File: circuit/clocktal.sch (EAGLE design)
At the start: 28 parts, among them IC1 PIC16F688, Q1 8.0

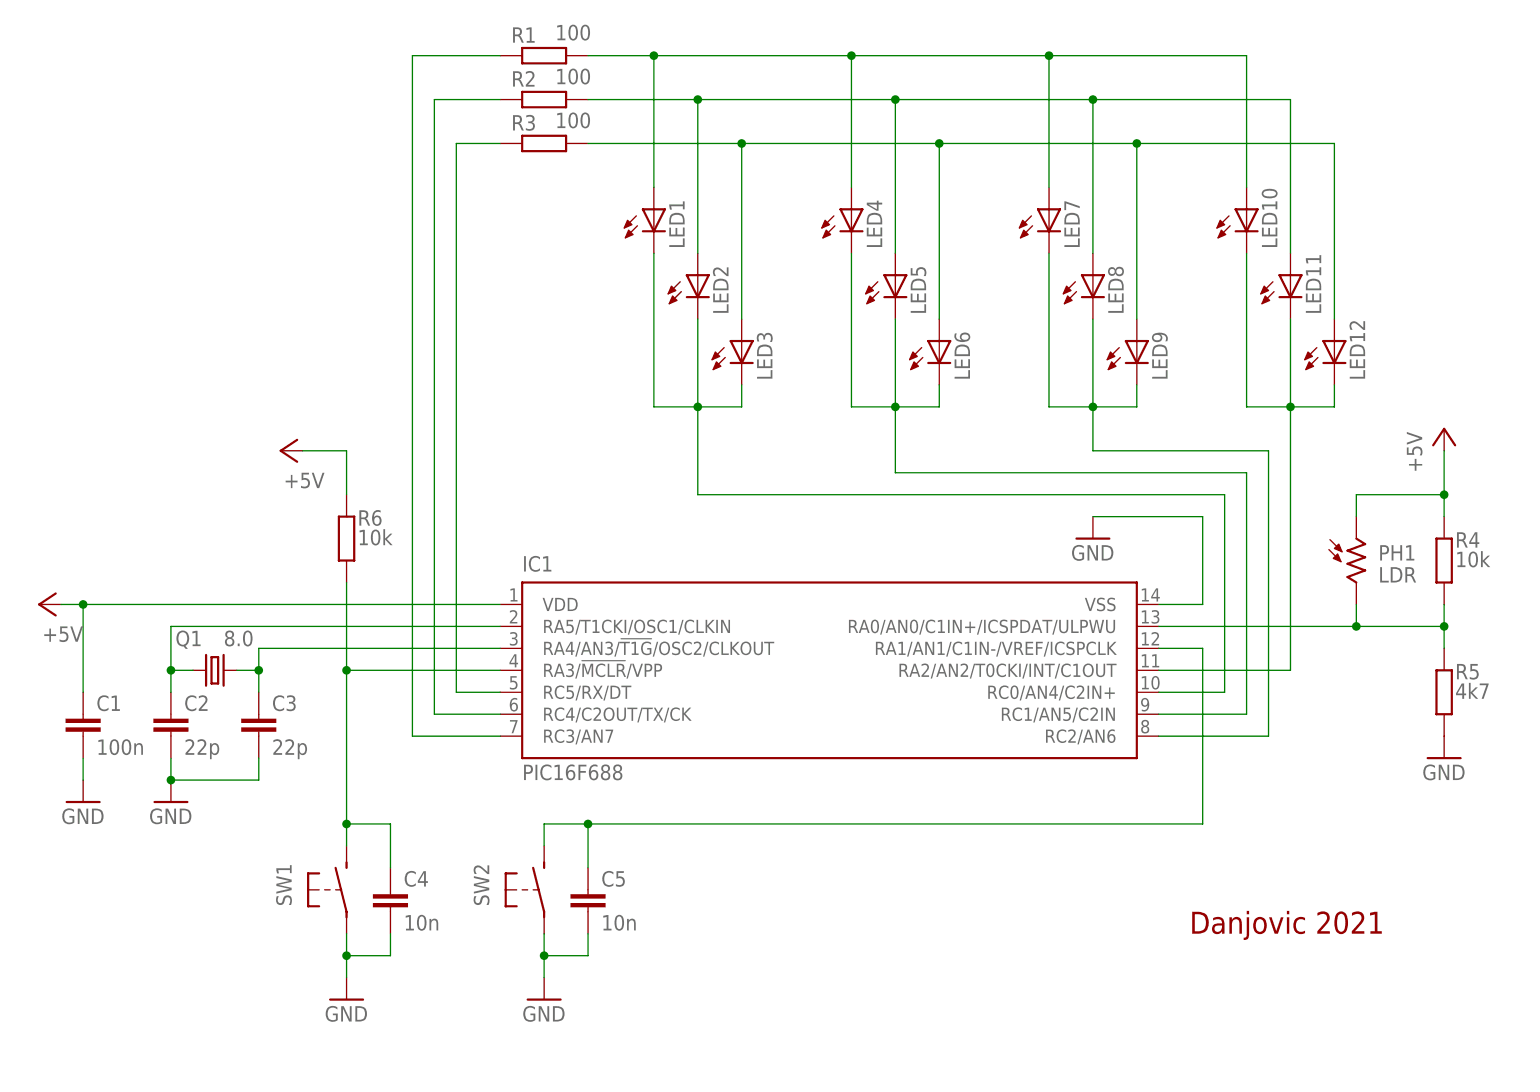
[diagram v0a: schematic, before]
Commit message: added Single Sided PCB design
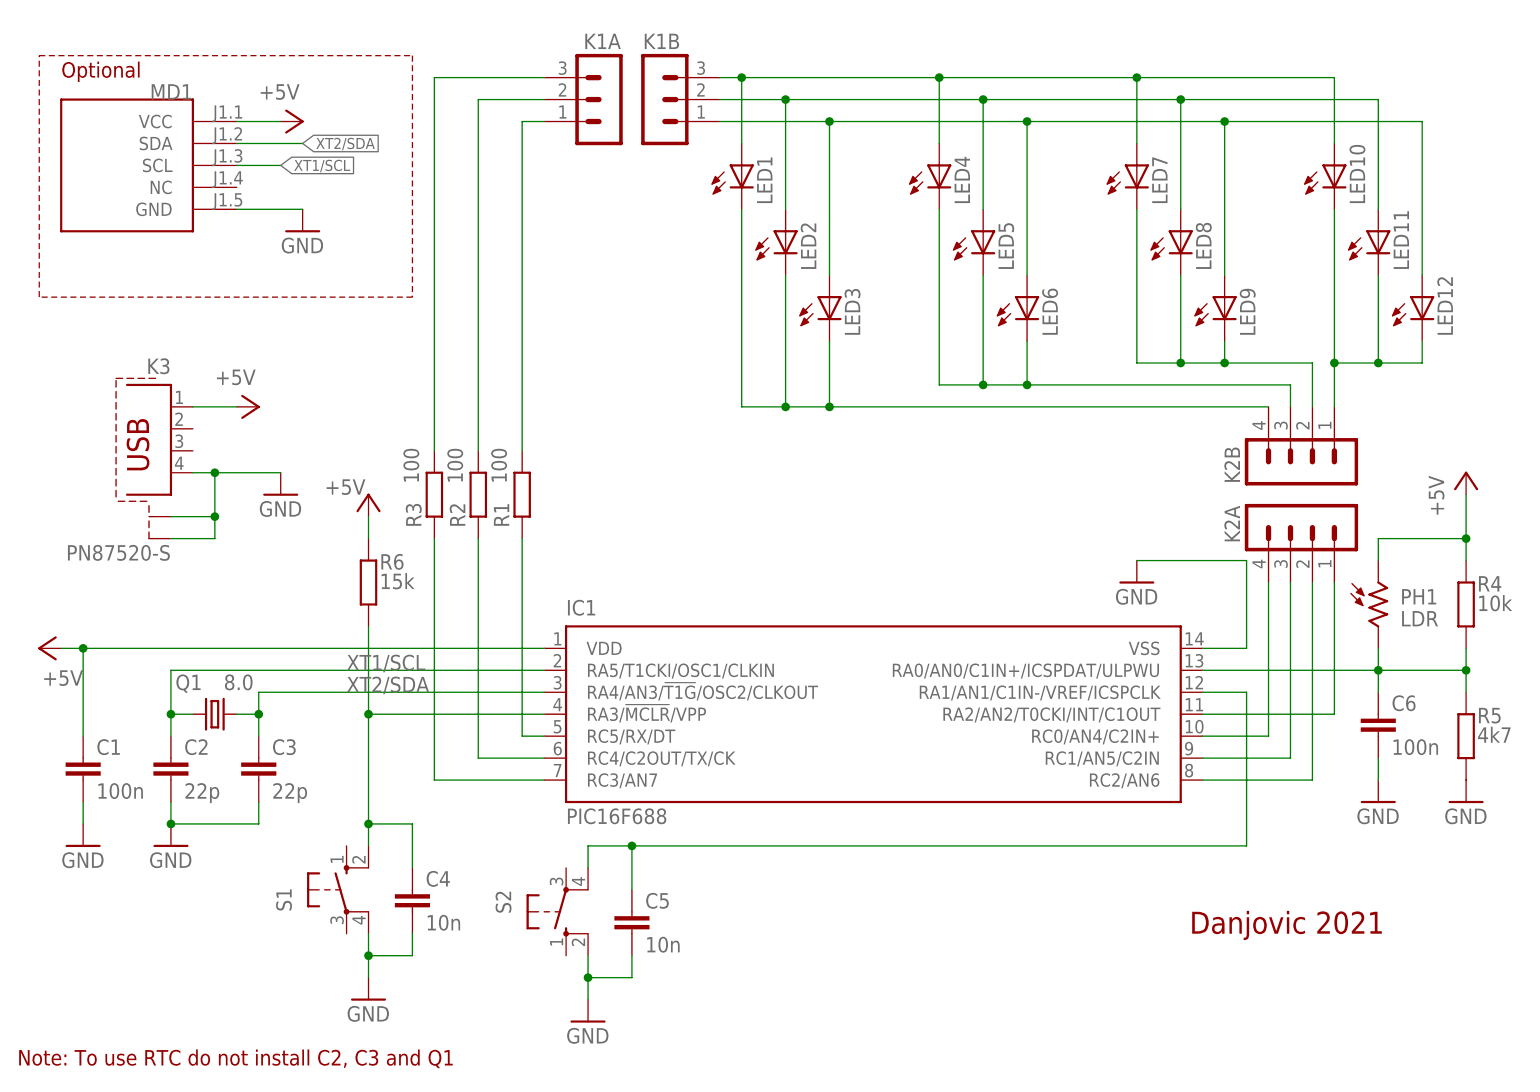
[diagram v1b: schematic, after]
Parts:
- removed SW1, SW2: (no value), tactile:MINISPDT
- added C6: 100n, rcl:C-EUC050-025X075L
- added K1A, K1B: (no value), con-lstb:MA03-1
- added K2A, K2B: (no value), con-lstb:MA04-1
- added K3: PN87520-S, con-berg:PN87520-S
- added MD1: (no value), RTC:RTC-DS3231_L
- added S1, S2: (no value), switch-omron:10-XX
- C1, C4, C5: device rcl:C-EU050-024X044 -> rcl:C-EUC050-025X075L
- C2, C3: device rcl:C-EU025-024X044 -> rcl:C-EUC050-024X044L
- LED1, LED10, LED11, LED12, LED2, LED3, LED4, LED5, LED6, LED7, LED8, LED9: device led:LED3MM -> led:LED3MM_L
- R1, R2, R3, R4, R5: device rcl:R-EU_0204/7 -> rcl:R-EU_0204/7L
- R6: value 10k -> 15k; device rcl:R-EU_0204/7 -> rcl:R-EU_0204/7L
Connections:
- removed net XT1: C2.1, IC1.RA5/T1CKI/OSC1/CLKIN, Q1.1
- removed net XT2: C3.1, IC1.RA4/AN3/!T1G!/OSC2/CLKOUT, Q1.2
- new net BIT0A: K1A.1, R1.2
- new net BIT1A: K1A.2, R2.2
- new net BIT2A: K1A.3, R3.2
- new net DGT0: K2B.1, LED10.C, LED11.C, LED12.C
- new net DGT1: K2B.2, LED7.C, LED8.C, LED9.C
- new net DGT2: K2B.3, LED4.C, LED5.C, LED6.C
- new net DGT3: K2B.4, LED1.C, LED2.C, LED3.C
- new net XT1/SCL: C2.1, IC1.RA5/T1CKI/OSC1/CLKIN, MD1.SCL, Q1.1
- new net XT2/SDA: C3.1, IC1.RA4/AN3/!T1G!/OSC2/CLKOUT, MD1.SDA, Q1.2
- net +5V: now also K3.1, MD1.VCC
- net B0: now also K1B.1; no longer R3.2
- net B1: now also K1B.2; no longer R2.2
- net B2: now also K1B.3; no longer R1.2
- net BIT0: now also R1.1; no longer R3.1
- net BIT2: now also R3.1; no longer R1.1
- net BUTTON1: now also S1.S1; no longer SW1.S
- net BUTTON2: now also S2.P1; no longer SW2.S
- net DIGIT0: now also K2A.1; no longer LED10.C, LED11.C, LED12.C
- net DIGIT1: now also K2A.2; no longer LED7.C, LED8.C, LED9.C
- net DIGIT2: now also K2A.3; no longer LED4.C, LED5.C, LED6.C
- net DIGIT3: now also K2A.4; no longer LED1.C, LED2.C, LED3.C
- net GND: now also C6.2, K3.4, K3.S1, K3.S2, MD1.GND, S1.P1, S2.S1; no longer SW1.P, SW2.P
- net LDR: now also C6.1
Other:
- note added: "Note: To use RTC do not install C2, C3 and Q1"
- note added: "Optional"
- moved on the sheet: C1, C2, C3, C4, C5, IC1, LED1, LED10, LED11, LED12, LED2, LED3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
